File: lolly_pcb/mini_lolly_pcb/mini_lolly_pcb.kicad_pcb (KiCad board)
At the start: 2 copper layers, 64 parts

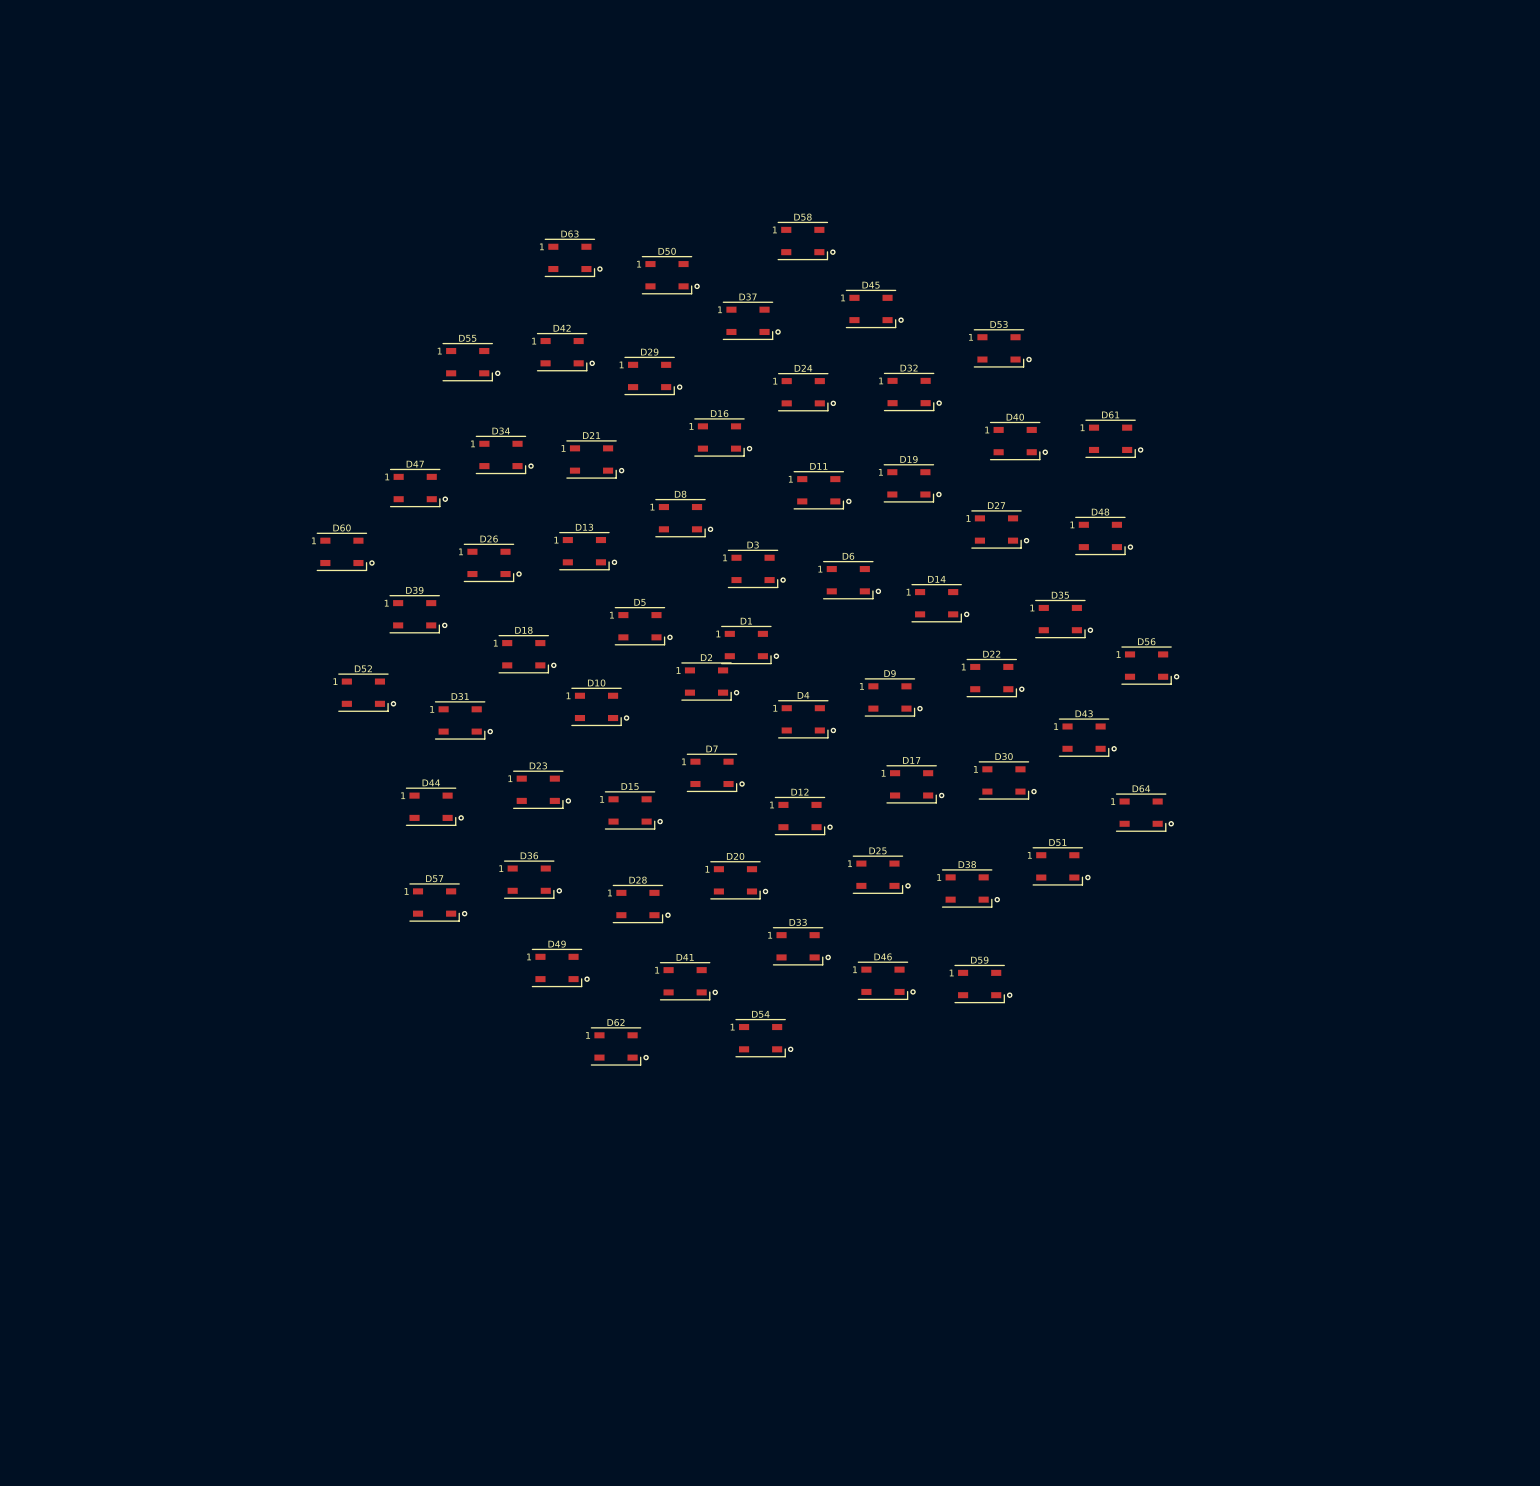
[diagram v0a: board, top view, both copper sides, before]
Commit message: add tracks and vias
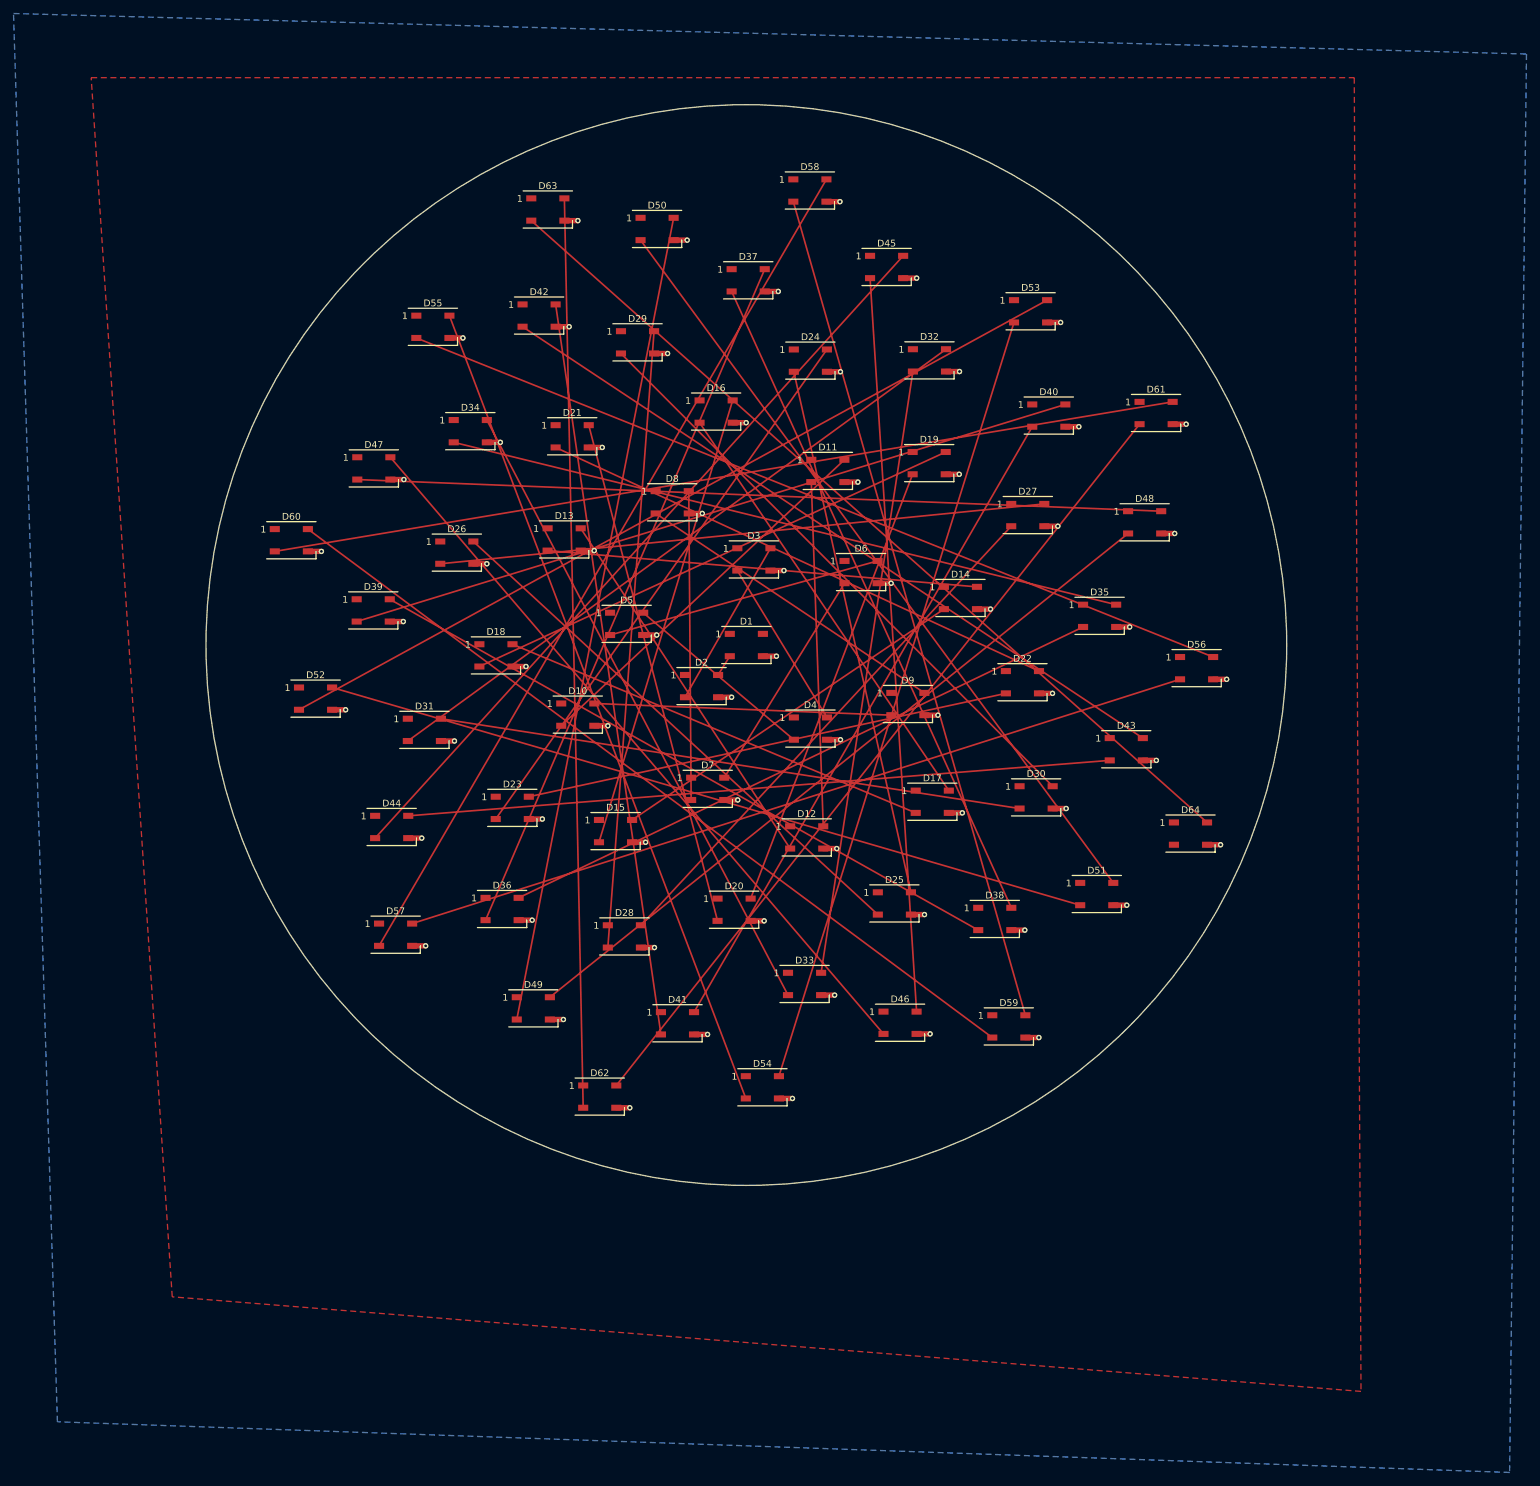
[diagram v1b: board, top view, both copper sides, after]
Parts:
- moved D64 7.94 mm to (215.8, 127.9)
- moved D63 7.87 mm to (120.6, 35.5)
- moved D62 7.81 mm to (128.3, 166.9)
- moved D61 7.75 mm to (210.7, 65.7)
- moved D60 7.68 mm to (82.6, 84.5)
- moved D59 7.62 mm to (188.9, 156.5)
- moved D58 7.55 mm to (159.4, 32.7)
- moved D57 7.48 mm to (98.1, 142.9)
- moved D56 7.42 mm to (216.7, 103.4)
- moved D55 7.35 mm to (103.6, 52.9)
- moved D54 7.28 mm to (152.4, 165.5)
- moved D53 7.21 mm to (192.1, 50.6)
- moved D52 7.14 mm to (86.2, 107.9)
- moved D51 7.07 mm to (201.9, 136.9)
- moved D50 7.00 mm to (136.8, 38.4)
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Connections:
- D1 pad 2: unconnected-(D1-DOUT-Pad2) -> Net-(D1-DOUT)
- D2 pad 4: unconnected-(D2-DIN-Pad4) -> Net-(D1-DOUT)
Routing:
- net Net-(D60-DOUT): track 0.00 -> 134.8 mm
- net Net-(D62-DOUT): track 0.00 -> 134.7 mm
- net Net-(D63-DOUT): track 0.00 -> 134.0 mm
- net Net-(D57-DOUT): track 0.00 -> 131.4 mm
- net GND: track 0.00 -> 128.0 mm
- net Net-(D55-DOUT): track 0.00 -> 127.1 mm
- net Net-(D52-DOUT): track 0.00 -> 126.3 mm
- net Net-(D59-DOUT): track 0.00 -> 126.2 mm
- net Net-(D58-DOUT): track 0.00 -> 125.3 mm
- net Net-(D61-DOUT): track 0.00 -> 124.8 mm
- net Net-(D54-DOUT): track 0.00 -> 123.9 mm
- net Net-(D49-DOUT): track 0.00 -> 120.9 mm
- net Net-(D56-DOUT): track 0.00 -> 119.3 mm
- net Net-(D47-DOUT): track 0.00 -> 119.1 mm
- net Net-(D50-DOUT): track 0.00 -> 118.1 mm
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- added copper zone on B.Cu, net GND
- added copper zone on F.Cu, net VCC
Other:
- board outline added: 160 x 160 mm

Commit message: rotate outermost leds for space
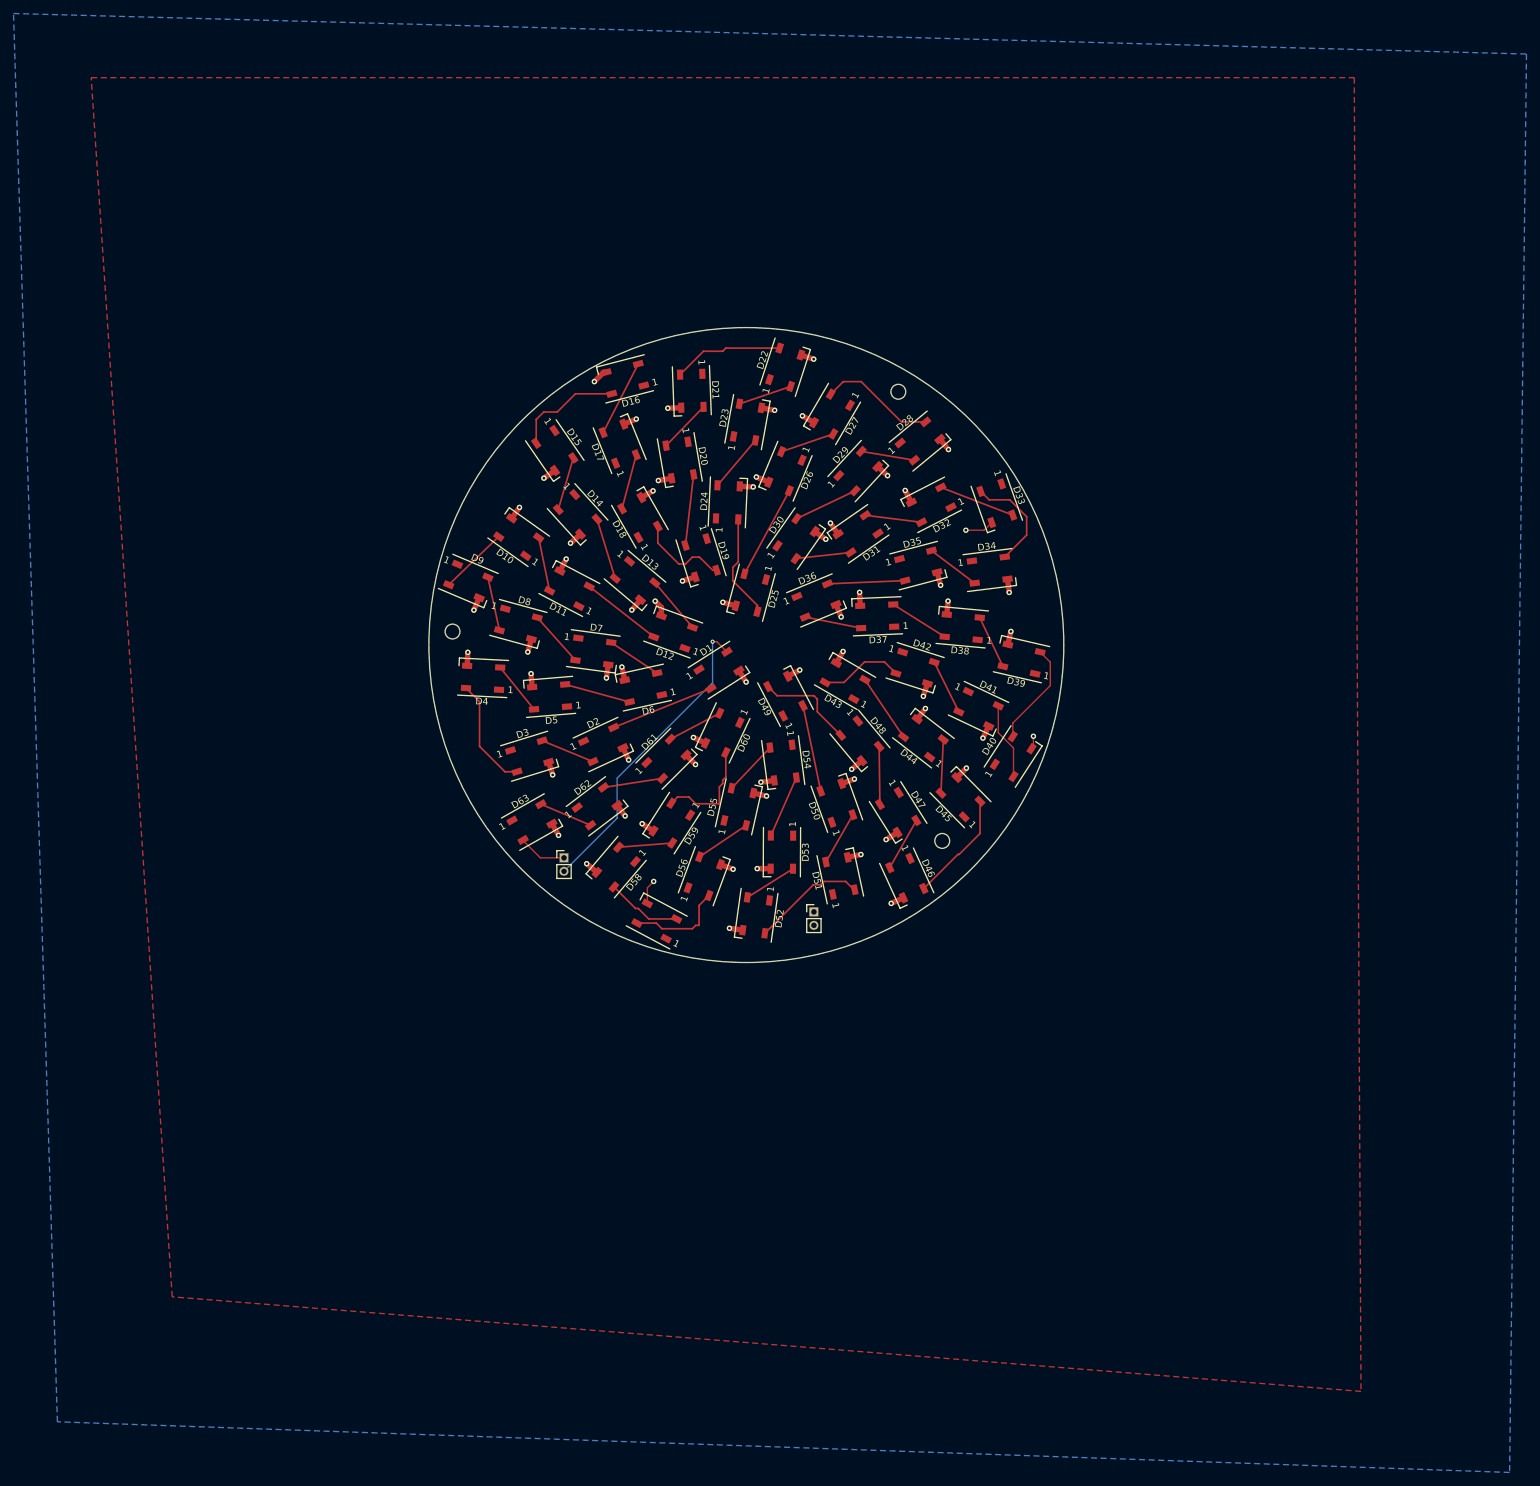
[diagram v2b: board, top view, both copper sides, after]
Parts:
- removed D64: WS2812B, LED_SMD:LED_WS2812B_PLCC4_5.0x5.0mm_P3.2mm
- added REF**: PinHeader_1x02_P2.00mm_Vertical, Connector_PinHeader_2.00mm:PinHeader_1x02_P2.00mm_Vertical, F.Cu at (160.0, 139.5)
- added REF**: MountingHole_2.2mm_M2, MountingHole:MountingHole_2.2mm_M2, F.Cu at (172.5, 62.5)
- added REF**: MountingHole_2.2mm_M2, MountingHole:MountingHole_2.2mm_M2, F.Cu at (179.0, 129.0)
- added REF**: PinHeader_1x02_P2.00mm_Vertical, Connector_PinHeader_2.00mm:PinHeader_1x02_P2.00mm_Vertical, F.Cu at (123.0, 131.5)
- added REF**: MountingHole_2.2mm_M2, MountingHole:MountingHole_2.2mm_M2, F.Cu at (106.5, 98.0)
- moved D58 104.2 mm to (130.7, 132.9), turned to -130.384 degrees
- moved D39 96.2 mm to (190.7, 102.1), turned to 167.06 degrees
- moved D47 92.8 mm to (172.5, 124.8), turned to -57.796 degrees
- moved D63 90.7 mm to (118.3, 126.2), turned to 29.552 degrees
- moved D50 89.0 mm to (163.4, 123.4), turned to 109.808 degrees
- moved D61 88.7 mm to (138.2, 116.8), turned to 44.888 degrees
- moved D53 88.1 mm to (155.3, 130.7), turned to -90.256 degrees
- moved D28 85.4 mm to (175.7, 69.8), turned to 39.584 degrees
- moved D55 84.3 mm to (148.9, 123.9), turned to 77.348 degrees
- moved D44 79.8 mm to (176.2, 113.8), turned to 142.268 degrees
- moved D34 79.6 mm to (186.0, 88.9), turned to 7.124 degrees
- moved D45 79.3 mm to (181.7, 122.5), turned to 134.6 degrees
- moved D56 79.1 mm to (143.8, 134.2), turned to 69.68 degrees
- moved D33 76.6 mm to (187.1, 79.0), turned to -70.48 degrees
- moved D42 76.3 mm to (175.0, 103.4), turned to -17.668 degrees
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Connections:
- D63 pad 2: Net-(D63-DOUT) -> unconnected-(D63-DOUT-Pad2)
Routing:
- net Net-(D63-DOUT): track 134.0 -> 0.00 mm
- net Net-(D62-DOUT): track 134.7 -> 8.00 mm
- net Net-(D60-DOUT): track 134.8 -> 8.26 mm
- net Net-(D57-DOUT): track 131.4 -> 11.2 mm
- net Net-(D55-DOUT): track 127.1 -> 8.32 mm
- net Net-(D52-DOUT): track 126.3 -> 7.97 mm
- net Net-(D58-DOUT): track 125.3 -> 7.99 mm
- net Net-(D61-DOUT): track 124.8 -> 8.84 mm
- net Net-(D54-DOUT): track 123.9 -> 8.27 mm
- net Net-(D47-DOUT): track 119.1 -> 8.59 mm
- net Net-(D59-DOUT): track 126.2 -> 15.9 mm
- net Net-(D50-DOUT): track 118.1 -> 8.06 mm
- net Net-(D44-DOUT): track 116.4 -> 7.97 mm
- net Net-(D49-DOUT): track 120.9 -> 12.9 mm
- net Net-(D53-DOUT): track 116.9 -> 9.38 mm
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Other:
- board size 160 x 160 mm -> 94 x 94 mm
- board text added: "Mini Lolly V1"
